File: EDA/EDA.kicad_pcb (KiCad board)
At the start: 2 copper layers, 75.4 x 53.8 mm, 38 parts, among them J2 Screw_Terminal_01x02, M1 Motor_Servo, U1 PMCF8316A1VRGFR, U2 LM2596S-5, U3 LM2678S-5

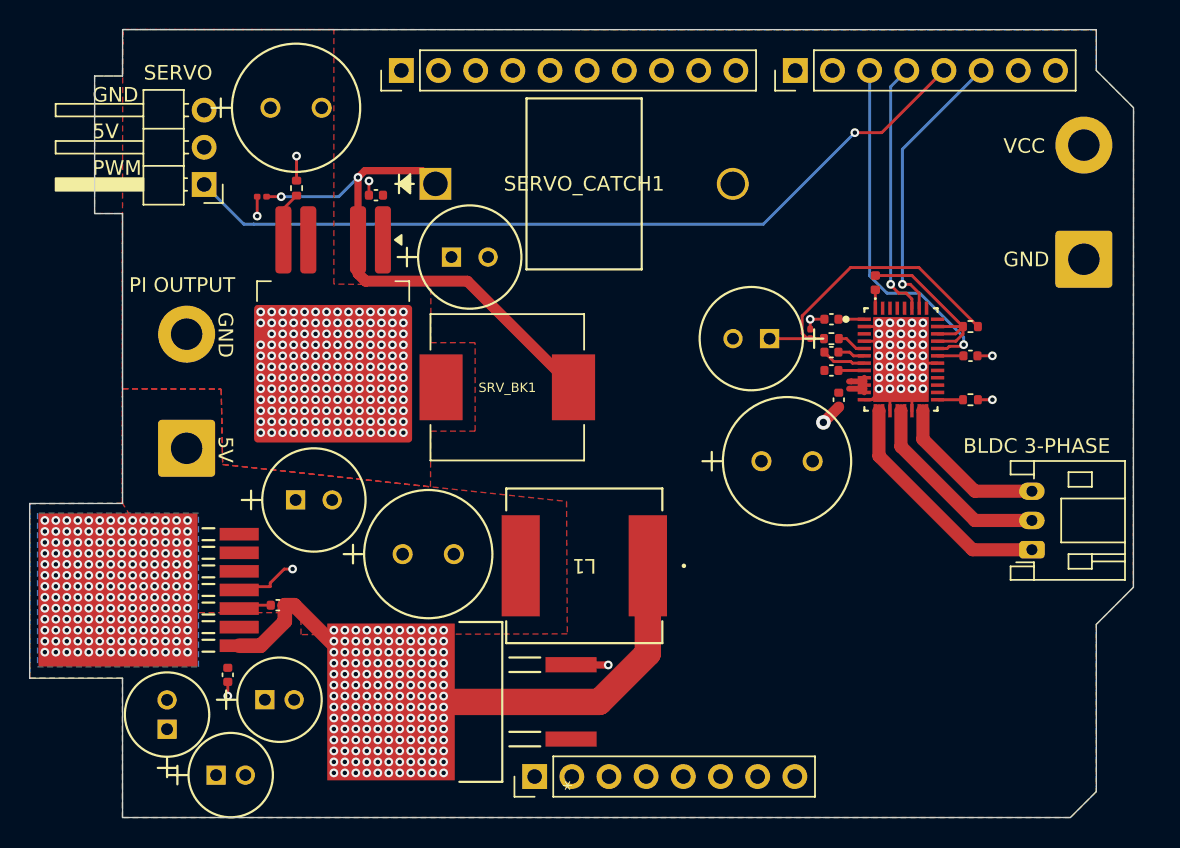
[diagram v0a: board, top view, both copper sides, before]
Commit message: Started Routing PCB.
- Developed Pi 5V, 5A power supply.
- Working on 5V, 3A servo power supply.
- Yet to begin wiring BLDC motor controller logic.
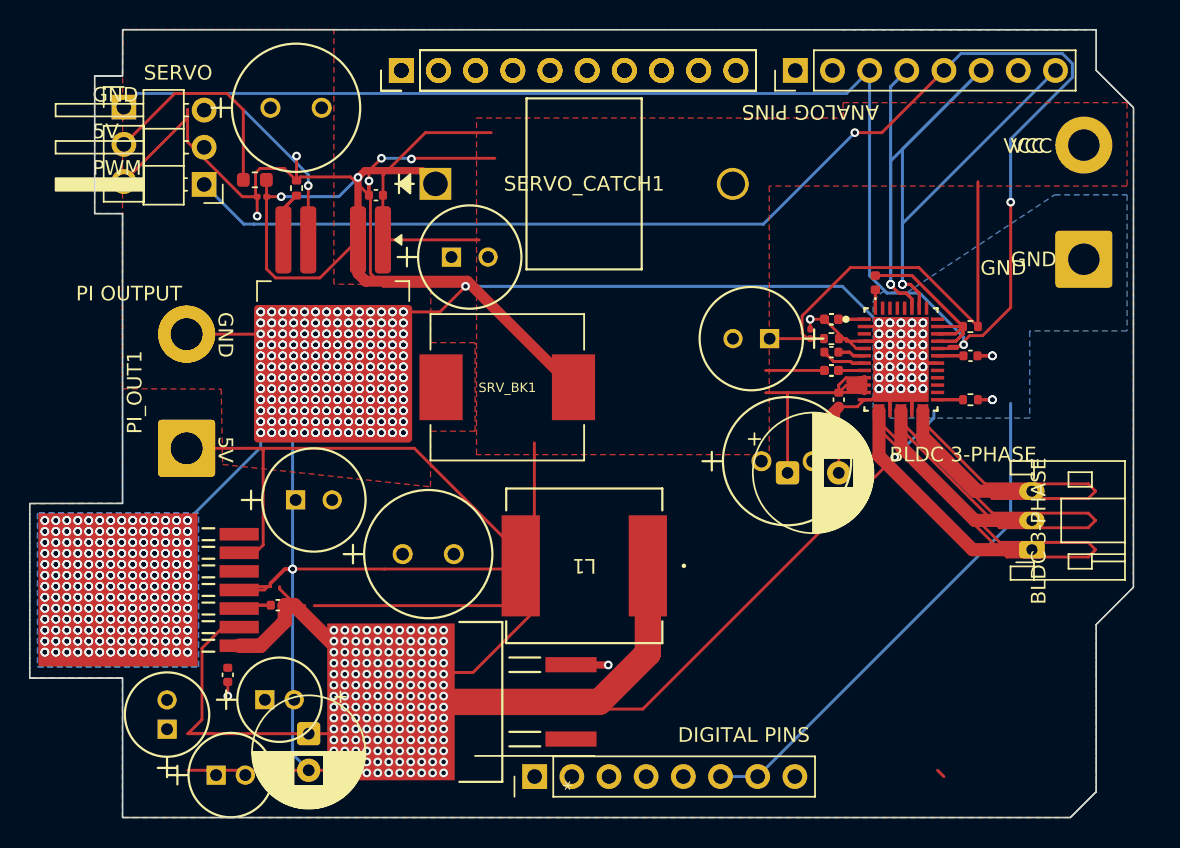
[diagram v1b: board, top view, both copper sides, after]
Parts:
- removed the ARD_B1 at (124.9, 73.8)
- removed the C_PUMP1 at (154.2, 94.2)
- removed the DVDD_BYP1 at (154.2, 90.8)
- removed the PI_OUT1 at (110.2, 99.6)
- added ARD_B1 (x2): Conn_01x10_Pin, Connector_PinHeader_2.54mm:PinHeader_1x10_P2.54mm_Vertical, F.Cu at (124.9, 73.8)
- added BULK_VM1: 500uf, Capacitor_THT:CP_Radial_D8.0mm_P3.50mm, F.Cu at (151.2, 101.2)
- added C_PUMP1 (x2): 1uf, Capacitor_SMD:C_0402_1005Metric, F.Cu at (154.2, 94.2)
- added DVDD_BYP1 (x2): 1uf, Capacitor_SMD:C_0402_1005Metric, F.Cu at (154.2, 90.8)
- added M1: Motor_Servo, Connector_PinHeader_2.54mm:PinHeader_1x03_P2.54mm_Vertical, F.Cu at (105.9, 76.3)
- added PI_BULK_A1: 15uf, Capacitor_THT:CP_Radial_D7.5mm_P2.50mm, F.Cu at (118.5, 119.1)
- added PI_OUT1 (x2): Screw_Terminal_01x02, Connector_Wire:SolderWire-1.5sqmm_1x02_P7.8mm_D1.7mm_OD3.9mm, F.Cu at (110.2, 99.6)
- added SRV_BK1: 47uh, Inductor_SMD:L_0603_1608Metric, F.Cu at (114.8, 81.2)
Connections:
- U1 pad 5: Net-(U1-SW_BK) -> unconnected-(U1-SW_BK-Pad5)
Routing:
- net GND: track 26.3 -> 282.8 mm, vias 394 -> 786
- net +7.5V: track 3.10 -> 103.0 mm
- net 63: track 0.00 -> 52.1 mm
- net SRV_PWM: track 56.0 -> 108.0 mm
- net SRV 5V, 3A: track 0.00 -> 39.0 mm
- net Net-(U2-~{ON}/OFF): track 3.40 -> 37.8 mm
- net Net-(ARD_C1-Pin_3): track 24.6 -> 58.7 mm, vias 1 -> 2
- net Net-(D_FAULT1-A): track 13.6 -> 43.3 mm
- net PI 5V, 5A: track 0.00 -> 25.6 mm, vias 0 -> 1
- net unconnected-(ARD_C1-Pin_8-Pad8): track 0.00 -> 21.4 mm, vias 0 -> 1
- net Net-(ARD_C1-Pin_6): track 19.3 -> 39.0 mm, vias 1 -> 2
- net Net-(U2-OUT): track 37.2 -> 50.8 mm
- net unconnected-(U1-FB_BK-Pad3): track 0.00 -> 13.6 mm
- net unconnected-(U3-NC-Pad5): track 0.00 -> 8.12 mm
- net unconnected-(PI_CATCH1-N/C-Pad1): track 0.00 -> 3.40 mm
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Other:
- board text added: "ANALOG PINS"
- board text added: "DIGITAL PINS"
- board text added: "SERVO OUT"
